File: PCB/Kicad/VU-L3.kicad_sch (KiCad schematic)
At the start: 32 parts, among them U5 SR1-L3, U6 SR2-L3

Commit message: PDF
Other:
- note added: "VU LINE 3"
- moved on the sheet: D46, D47, D48, D49, D50, D51, D52, D53, D54, D55, D56, D57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

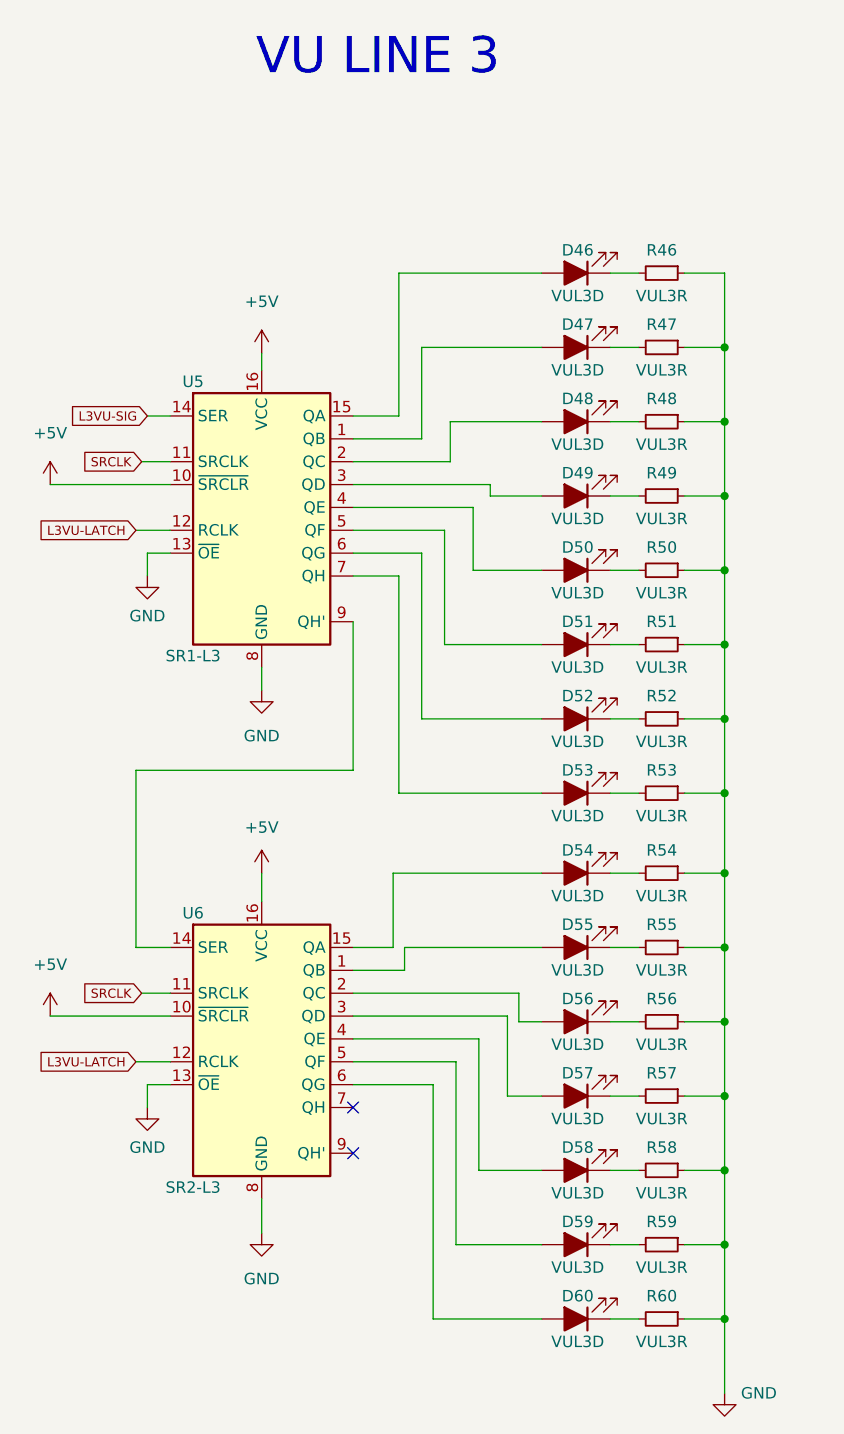
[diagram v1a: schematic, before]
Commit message: added transistor and 3x leds play- cue
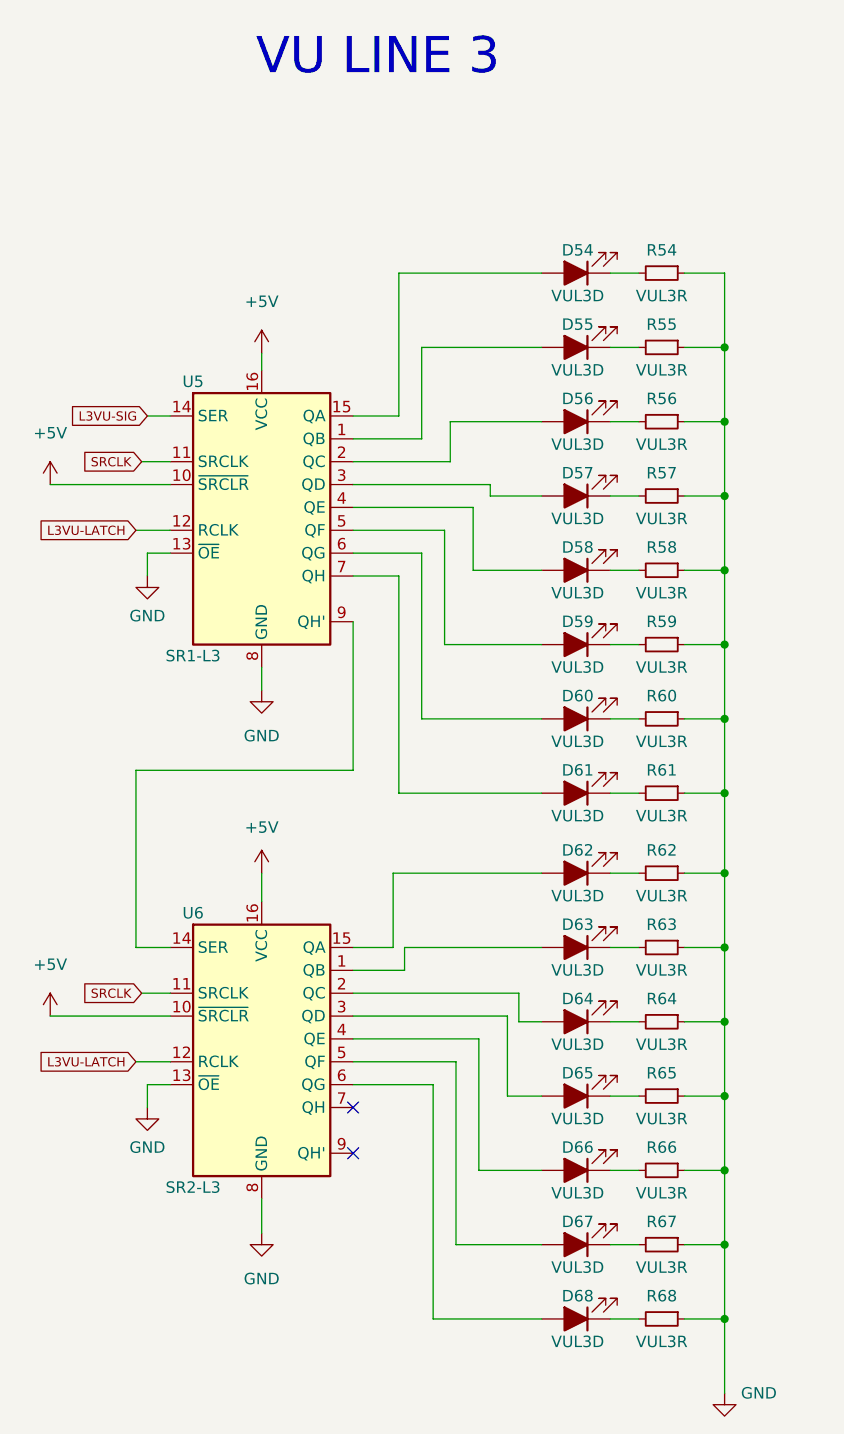
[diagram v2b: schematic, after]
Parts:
- U5, U6: footprint (none) -> Library:SO-16_3.9x9.9mm_P1.27mm
- renumbered D46 to D54, D47 to D55, D48 to D56, D49 to D57, D50 to D58, D51 to D59, D52 to D60, D53 to D61, D54 to D62, D55 to D63, D56 to D64, D57 to D65, D58 to D66, D59 to D67, D60 to D68, R46 to R54, R47 to R55, R48 to R56, R49 to R57, R50 to R58, R51 to R59, R52 to R60, R53 to R61, R54 to R62, R55 to R63, R56 to R64, R57 to R65, R58 to R66, R59 to R67, R60 to R68

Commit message: routing WIP
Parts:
- D63, D64, D65, D66: footprint Library:LED_GREEN -> Library:LED_YELLOW
- D67, D68: footprint Library:LED_GREEN -> Library:LED_RED
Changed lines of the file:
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@@
     (property "Reference" "D63" (id 0) (at 117.0305 130.175 0))
     (property "Value" "VUL3D" (id 1) (at 117.0305 135.255 0))
-    (property "Footprint" "Library:LED_GREEN" (id 2) (at 116.84 132.715 0)
+    (property "Footprint" "Library:LED_YELLOW" (id 2) (at 116.84 132.715 0)
       (effects (font (size 1.27 1.27)) hide)
     )
@@
     (property "Reference" "D64" (id 0) (at 117.0305 138.43 0))
     (property "Value" "VUL3D" (id 1) (at 117.0305 143.51 0))
-    (property "Footprint" "Library:LED_GREEN" (id 2) (at 116.84 140.97 0)
+    (property "Footprint" "Library:LED_YELLOW" (id 2) (at 116.84 140.97 0)
       (effects (font (size 1.27 1.27)) hide)
     )
@@
     (property "Reference" "D65" (id 0) (at 117.0305 146.685 0))
     (property "Value" "VUL3D" (id 1) (at 117.0305 151.765 0))
-    (property "Footprint" "Library:LED_GREEN" (id 2) (at 116.84 149.225 0)
+    (property "Footprint" "Library:LED_YELLOW" (id 2) (at 116.84 149.225 0)
       (effects (font (size 1.27 1.27)) hide)
     )
@@
     (property "Reference" "D66" (id 0) (at 117.0305 154.94 0))
     (property "Value" "VUL3D" (id 1) (at 117.0305 160.02 0))
-    (property "Footprint" "Library:LED_GREEN" (id 2) (at 116.84 157.48 0)
+    (property "Footprint" "Library:LED_YELLOW" (id 2) (at 116.84 157.48 0)
       (effects (font (size 1.27 1.27)) hide)
     )
@@
     (property "Reference" "D67" (id 0) (at 117.0305 163.195 0))
     (property "Value" "VUL3D" (id 1) (at 117.0305 168.275 0))
-    (property "Footprint" "Library:LED_GREEN" (id 2) (at 116.84 165.735 0)
+    (property "Footprint" "Library:LED_RED" (id 2) (at 116.84 165.735 0)
       (effects (font (size 1.27 1.27)) hide)
     )
@@
     (property "Reference" "D68" (id 0) (at 117.0305 171.45 0))
     (property "Value" "VUL3D" (id 1) (at 117.0305 176.53 0))
-    (property "Footprint" "Library:LED_GREEN" (id 2) (at 116.84 173.99 0)
+    (property "Footprint" "Library:LED_RED" (id 2) (at 116.84 173.99 0)
       (effects (font (size 1.27 1.27)) hide)
     )

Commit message: routes finished
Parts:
- D54, D55: footprint Library:LED_GREEN -> Library:LED_RED
- D56, D57, D58, D59: footprint Library:LED_GREEN -> Library:LED_YELLOW
- D63, D64, D65, D66: footprint Library:LED_YELLOW -> Library:LED_GREEN
- D67, D68: footprint Library:LED_RED -> Library:LED_GREEN
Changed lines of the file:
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@@
-(kicad_sch (version 20210615) (generator eeschema)
+(kicad_sch (version 20210621) (generator eeschema)
   (paper "A4")
   (junction (at 133.35 66.04) (diameter 0.9144) (color 0 0 0 0))
@@
     (property "Reference" "D54" (id 0) (at 117.0305 55.245 0))
     (property "Value" "VUL3D" (id 1) (at 117.0305 60.325 0))
-    (property "Footprint" "Library:LED_GREEN" (id 2) (at 116.84 57.785 0)
+    (property "Footprint" "Library:LED_RED" (id 2) (at 116.84 57.785 0)
       (effects (font (size 1.27 1.27)) hide)
     )
@@
     (property "Reference" "D55" (id 0) (at 117.0305 63.5 0))
     (property "Value" "VUL3D" (id 1) (at 117.0305 68.58 0))
-    (property "Footprint" "Library:LED_GREEN" (id 2) (at 116.84 66.04 0)
+    (property "Footprint" "Library:LED_RED" (id 2) (at 116.84 66.04 0)
       (effects (font (size 1.27 1.27)) hide)
     )
@@
     (property "Reference" "D56" (id 0) (at 117.0305 71.755 0))
     (property "Value" "VUL3D" (id 1) (at 117.0305 76.835 0))
-    (property "Footprint" "Library:LED_GREEN" (id 2) (at 116.84 74.295 0)
+    (property "Footprint" "Library:LED_YELLOW" (id 2) (at 116.84 74.295 0)
       (effects (font (size 1.27 1.27)) hide)
     )
@@
     (property "Reference" "D57" (id 0) (at 117.0305 80.01 0))
     (property "Value" "VUL3D" (id 1) (at 117.0305 85.09 0))
-    (property "Footprint" "Library:LED_GREEN" (id 2) (at 116.84 82.55 0)
+    (property "Footprint" "Library:LED_YELLOW" (id 2) (at 116.84 82.55 0)
       (effects (font (size 1.27 1.27)) hide)
     )
@@
     (property "Reference" "D58" (id 0) (at 117.0305 88.265 0))
     (property "Value" "VUL3D" (id 1) (at 117.0305 93.345 0))
-    (property "Footprint" "Library:LED_GREEN" (id 2) (at 116.84 90.805 0)
+    (property "Footprint" "Library:LED_YELLOW" (id 2) (at 116.84 90.805 0)
       (effects (font (size 1.27 1.27)) hide)
     )
@@
     (property "Reference" "D59" (id 0) (at 117.0305 96.52 0))
     (property "Value" "VUL3D" (id 1) (at 117.0305 101.6 0))
-    (property "Footprint" "Library:LED_GREEN" (id 2) (at 116.84 99.06 0)
+    (property "Footprint" "Library:LED_YELLOW" (id 2) (at 116.84 99.06 0)
       (effects (font (size 1.27 1.27)) hide)
     )
@@
     (property "Reference" "D63" (id 0) (at 117.0305 130.175 0))
     (property "Value" "VUL3D" (id 1) (at 117.0305 135.255 0))
-    (property "Footprint" "Library:LED_YELLOW" (id 2) (at 116.84 132.715 0)
+    (property "Footprint" "Library:LED_GREEN" (id 2) (at 116.84 132.715 0)
       (effects (font (size 1.27 1.27)) hide)
     )
@@
     (property "Reference" "D64" (id 0) (at 117.0305 138.43 0))
     (property "Value" "VUL3D" (id 1) (at 117.0305 143.51 0))
-    (property "Footprint" "Library:LED_YELLOW" (id 2) (at 116.84 140.97 0)
+    (property "Footprint" "Library:LED_GREEN" (id 2) (at 116.84 140.97 0)
       (effects (font (size 1.27 1.27)) hide)
     )
@@
     (property "Reference" "D65" (id 0) (at 117.0305 146.685 0))
     (property "Value" "VUL3D" (id 1) (at 117.0305 151.765 0))
-    (property "Footprint" "Library:LED_YELLOW" (id 2) (at 116.84 149.225 0)
+    (property "Footprint" "Library:LED_GREEN" (id 2) (at 116.84 149.225 0)
       (effects (font (size 1.27 1.27)) hide)
     )
@@
     (property "Reference" "D66" (id 0) (at 117.0305 154.94 0))
     (property "Value" "VUL3D" (id 1) (at 117.0305 160.02 0))
-    (property "Footprint" "Library:LED_YELLOW" (id 2) (at 116.84 157.48 0)
+    (property "Footprint" "Library:LED_GREEN" (id 2) (at 116.84 157.48 0)
       (effects (font (size 1.27 1.27)) hide)
     )
@@
     (property "Reference" "D67" (id 0) (at 117.0305 163.195 0))
     (property "Value" "VUL3D" (id 1) (at 117.0305 168.275 0))
-    (property "Footprint" "Library:LED_RED" (id 2) (at 116.84 165.735 0)
+    (property "Footprint" "Library:LED_GREEN" (id 2) (at 116.84 165.735 0)
       (effects (font (size 1.27 1.27)) hide)
     )
@@
     (property "Reference" "D68" (id 0) (at 117.0305 171.45 0))
     (property "Value" "VUL3D" (id 1) (at 117.0305 176.53 0))
-    (property "Footprint" "Library:LED_RED" (id 2) (at 116.84 173.99 0)
-      (effects (font (size 1.27 1.27)) hide)
-    )
+    (property "Footprint" "Library:LED_GREEN" (id 2) (at 116.84 173.99 0)
+      (effects (font (size 1.27 1.27)) hide)
+    )

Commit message: update schematic
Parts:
- R54, R55, R56, R57, R58, R59, R60, R61, R62, R63, R64, R65, R66, R67, R68: footprint Library:R_1206_3216Metric_Pad1.30x1.75mm_HandSolder -> Resistor_SMD:R_1206_3216Metric_Pad1.30x1.75mm_HandSolder
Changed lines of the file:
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@@
     (property "Reference" "R54" (id 0) (at 126.365 55.245 90))
     (property "Value" "VUL3R" (id 1) (at 126.365 60.325 90))
-    (property "Footprint" "Library:R_1206_3216Metric_Pad1.30x1.75mm_HandSolder" (id 2) (at 126.365 57.785 0)
+    (property "Footprint" "Resistor_SMD:R_1206_3216Metric_Pad1.30x1.75mm_HandSolder" (id 2) (at 126.365 57.785 0)
       (effects (font (size 1.27 1.27)) hide)
     )
@@
     (property "Reference" "R55" (id 0) (at 126.365 63.5 90))
     (property "Value" "VUL3R" (id 1) (at 126.365 68.58 90))
-    (property "Footprint" "Library:R_1206_3216Metric_Pad1.30x1.75mm_HandSolder" (id 2) (at 126.365 66.04 0)
+    (property "Footprint" "Resistor_SMD:R_1206_3216Metric_Pad1.30x1.75mm_HandSolder" (id 2) (at 126.365 66.04 0)
       (effects (font (size 1.27 1.27)) hide)
     )
@@
     (property "Reference" "R56" (id 0) (at 126.365 71.755 90))
     (property "Value" "VUL3R" (id 1) (at 126.365 76.835 90))
-    (property "Footprint" "Library:R_1206_3216Metric_Pad1.30x1.75mm_HandSolder" (id 2) (at 126.365 74.295 0)
+    (property "Footprint" "Resistor_SMD:R_1206_3216Metric_Pad1.30x1.75mm_HandSolder" (id 2) (at 126.365 74.295 0)
       (effects (font (size 1.27 1.27)) hide)
     )
@@
     (property "Reference" "R57" (id 0) (at 126.365 80.01 90))
     (property "Value" "VUL3R" (id 1) (at 126.365 85.09 90))
-    (property "Footprint" "Library:R_1206_3216Metric_Pad1.30x1.75mm_HandSolder" (id 2) (at 126.365 82.55 0)
+    (property "Footprint" "Resistor_SMD:R_1206_3216Metric_Pad1.30x1.75mm_HandSolder" (id 2) (at 126.365 82.55 0)
       (effects (font (size 1.27 1.27)) hide)
     )
@@
     (property "Reference" "R58" (id 0) (at 126.365 88.265 90))
     (property "Value" "VUL3R" (id 1) (at 126.365 93.345 90))
-    (property "Footprint" "Library:R_1206_3216Metric_Pad1.30x1.75mm_HandSolder" (id 2) (at 126.365 90.805 0)
+    (property "Footprint" "Resistor_SMD:R_1206_3216Metric_Pad1.30x1.75mm_HandSolder" (id 2) (at 126.365 90.805 0)
       (effects (font (size 1.27 1.27)) hide)
     )
@@
     (property "Reference" "R59" (id 0) (at 126.365 96.52 90))
     (property "Value" "VUL3R" (id 1) (at 126.365 101.6 90))
-    (property "Footprint" "Library:R_1206_3216Metric_Pad1.30x1.75mm_HandSolder" (id 2) (at 126.365 99.06 0)
+    (property "Footprint" "Resistor_SMD:R_1206_3216Metric_Pad1.30x1.75mm_HandSolder" (id 2) (at 126.365 99.06 0)
       (effects (font (size 1.27 1.27)) hide)
     )
@@
     (property "Reference" "R60" (id 0) (at 126.365 104.775 90))
     (property "Value" "VUL3R" (id 1) (at 126.365 109.855 90))
-    (property "Footprint" "Library:R_1206_3216Metric_Pad1.30x1.75mm_HandSolder" (id 2) (at 126.365 107.315 0)
+    (property "Footprint" "Resistor_SMD:R_1206_3216Metric_Pad1.30x1.75mm_HandSolder" (id 2) (at 126.365 107.315 0)
       (effects (font (size 1.27 1.27)) hide)
     )
@@
     (property "Reference" "R61" (id 0) (at 126.365 113.03 90))
     (property "Value" "VUL3R" (id 1) (at 126.365 118.11 90))
-    (property "Footprint" "Library:R_1206_3216Metric_Pad1.30x1.75mm_HandSolder" (id 2) (at 126.365 115.57 0)
+    (property "Footprint" "Resistor_SMD:R_1206_3216Metric_Pad1.30x1.75mm_HandSolder" (id 2) (at 126.365 115.57 0)
       (effects (font (size 1.27 1.27)) hide)
     )
@@
     (property "Reference" "R62" (id 0) (at 126.365 121.92 90))
     (property "Value" "VUL3R" (id 1) (at 126.365 127 90))
-    (property "Footprint" "Library:R_1206_3216Metric_Pad1.30x1.75mm_HandSolder" (id 2) (at 126.365 124.46 0)
+    (property "Footprint" "Resistor_SMD:R_1206_3216Metric_Pad1.30x1.75mm_HandSolder" (id 2) (at 126.365 124.46 0)
       (effects (font (size 1.27 1.27)) hide)
     )
@@
     (property "Reference" "R63" (id 0) (at 126.365 130.175 90))
     (property "Value" "VUL3R" (id 1) (at 126.365 135.255 90))
-    (property "Footprint" "Library:R_1206_3216Metric_Pad1.30x1.75mm_HandSolder" (id 2) (at 126.365 132.715 0)
+    (property "Footprint" "Resistor_SMD:R_1206_3216Metric_Pad1.30x1.75mm_HandSolder" (id 2) (at 126.365 132.715 0)
       (effects (font (size 1.27 1.27)) hide)
     )
@@
     (property "Reference" "R64" (id 0) (at 126.365 138.43 90))
     (property "Value" "VUL3R" (id 1) (at 126.365 143.51 90))
-    (property "Footprint" "Library:R_1206_3216Metric_Pad1.30x1.75mm_HandSolder" (id 2) (at 126.365 140.97 0)
+    (property "Footprint" "Resistor_SMD:R_1206_3216Metric_Pad1.30x1.75mm_HandSolder" (id 2) (at 126.365 140.97 0)
       (effects (font (size 1.27 1.27)) hide)
     )
@@
     (property "Reference" "R65" (id 0) (at 126.365 146.685 90))
     (property "Value" "VUL3R" (id 1) (at 126.365 151.765 90))
-    (property "Footprint" "Library:R_1206_3216Metric_Pad1.30x1.75mm_HandSolder" (id 2) (at 126.365 149.225 0)
+    (property "Footprint" "Resistor_SMD:R_1206_3216Metric_Pad1.30x1.75mm_HandSolder" (id 2) (at 126.365 149.225 0)
       (effects (font (size 1.27 1.27)) hide)
     )
@@
     (property "Reference" "R66" (id 0) (at 126.365 154.94 90))
     (property "Value" "VUL3R" (id 1) (at 126.365 160.02 90))
-    (property "Footprint" "Library:R_1206_3216Metric_Pad1.30x1.75mm_HandSolder" (id 2) (at 126.365 157.48 0)
+    (property "Footprint" "Resistor_SMD:R_1206_3216Metric_Pad1.30x1.75mm_HandSolder" (id 2) (at 126.365 157.48 0)
       (effects (font (size 1.27 1.27)) hide)
     )
@@
     (property "Reference" "R67" (id 0) (at 126.365 163.195 90))
     (property "Value" "VUL3R" (id 1) (at 126.365 168.275 90))
-    (property "Footprint" "Library:R_1206_3216Metric_Pad1.30x1.75mm_HandSolder" (id 2) (at 126.365 165.735 0)
+    (property "Footprint" "Resistor_SMD:R_1206_3216Metric_Pad1.30x1.75mm_HandSolder" (id 2) (at 126.365 165.735 0)
       (effects (font (size 1.27 1.27)) hide)
     )
@@
     (property "Reference" "R68" (id 0) (at 126.365 171.45 90))
     (property "Value" "VUL3R" (id 1) (at 126.365 176.53 90))
-    (property "Footprint" "Library:R_1206_3216Metric_Pad1.30x1.75mm_HandSolder" (id 2) (at 126.365 173.99 0)
+    (property "Footprint" "Resistor_SMD:R_1206_3216Metric_Pad1.30x1.75mm_HandSolder" (id 2) (at 126.365 173.99 0)
       (effects (font (size 1.27 1.27)) hide)
     )

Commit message: modified trillbar connectors
Signed-off-by: Jose Vega <josevega234@gmail.com>
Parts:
- U5, U6: footprint Library:SO-16_3.9x9.9mm_P1.27mm -> Package_SO:SOIC-16_3.9x9.9mm_P1.27mm
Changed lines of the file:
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@@
-(kicad_sch (version 20210621) (generator eeschema)
+(kicad_sch (version 20210615) (generator eeschema)
   (paper "A4")
   (junction (at 133.35 66.04) (diameter 0.9144) (color 0 0 0 0))
@@
     (property "Reference" "U5" (id 0) (at 74.295 69.85 0))
     (property "Value" "SR1-L3" (id 1) (at 74.295 100.33 0))
-    (property "Footprint" "Library:SO-16_3.9x9.9mm_P1.27mm" (id 2) (at 81.915 83.82 0)
+    (property "Footprint" "Package_SO:SOIC-16_3.9x9.9mm_P1.27mm" (id 2) (at 81.915 83.82 0)
       (effects (font (size 1.27 1.27)) hide)
     )
@@
     (property "Reference" "U6" (id 0) (at 74.295 128.905 0))
     (property "Value" "SR2-L3" (id 1) (at 74.295 159.385 0))
-    (property "Footprint" "Library:SO-16_3.9x9.9mm_P1.27mm" (id 2) (at 81.915 142.875 0)
-      (effects (font (size 1.27 1.27)) hide)
-    )
+    (property "Footprint" "Package_SO:SOIC-16_3.9x9.9mm_P1.27mm" (id 2) (at 81.915 142.875 0)
+      (effects (font (size 1.27 1.27)) hide)
+    )
